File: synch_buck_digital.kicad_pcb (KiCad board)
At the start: 4 copper layers, 60 x 60 mm, 48 parts, among them U1 BSC066N06NSATMA1, U2 BSC066N06NSATMA1, U3 INA241A3IDDFR

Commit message: Updated pcb
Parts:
- moved TP4 16.0 mm to (235.1, 87.3)
- moved TP1 13.0 mm to (208.0, 89.3)
- moved C_OC_100P1 11.2 mm to (190.9, 87.1)
- moved C_OC_10N1 11.2 mm to (192.4, 87.9)
- moved C_OC_1U1 11.2 mm to (193.9, 87.1)
- moved R_HYS1 11.2 mm to (192.1, 90.7)
- moved U_OC1 11.2 mm to (188.0, 89.0)
- moved J_STM1 11.1 mm to (192.0, 99.6)
- moved TP3 8.14 mm to (203.9, 89.3)
- moved C_VFB_FILT1 5.82 mm to (233.5, 92.0)
- moved R1_VFB1 5.82 mm to (230.5, 92.0)
- moved R2_VFB1 5.82 mm to (230.5, 87.4)
- moved D1 5.82 mm to (237.0, 92.9)
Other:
- board size 60 x 60 mm -> 60 x 49.6 mm
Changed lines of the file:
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@@
 	(footprint "Capacitor_SMD:C_0603_1608Metric"
 		(layer "F.Cu")
-		(at 233.83 97.8525 90)
+		(at 233.47 92.04 90)
 		(descr "Capacitor SMD 0603 (1608 Metric), square (rectangular) end terminal, IPC-7351 nominal, (Body size source: IPC-SM-782 page 76, https://www.pcb-3d.com/wordpress/wp-content/uploads/ipc-sm-782a_amendment_1_and_2.pdf)")
 		(tags "capacitor")
@@
 	(footprint "Connector_PinHeader_2.54mm:PinHeader_1x13_P2.54mm_Vertical"
 		(layer "F.Cu")
-		(at 195.48 110.21 90)
+		(at 192.04 99.63 90)
 		(descr "Through hole straight pin header, 1x13, 2.54mm pitch, single row")
 		(tags "Through hole pin header THT 1x13 2.54mm single row")
@@
 	(footprint "TLV3603:SC70_DCK_TEX"
 		(layer "F.Cu")
-		(at 187.90755 100.159999)
+		(at 188.03755 88.999999)
 		(tags "TLV3603DCKR-ET ")
 		(property "Reference" "U_OC1"
@@
 	(footprint "Resistor_SMD:R_0603_1608Metric"
 		(layer "F.Cu")
-		(at 230.83 93.2325 -90)
+		(at 230.47 87.42 -90)
 		(descr "Resistor SMD 0603 (1608 Metric), square (rectangular) end terminal, IPC-7351 nominal, (Body size source: IPC-SM-782 page 72, https://www.pcb-3d.com/wordpress/wp-content/uploads/ipc-sm-782a_amendment_1_and_2.pdf)")
 		(tags "resistor")
@@
 	(footprint "Capacitor_SMD:C_0805_2012Metric"
 		(layer "F.Cu")
-		(at 193.78 98.28 90)
+		(at 193.91 87.12 90)
 		(descr "Capacitor SMD 0805 (2012 Metric), square (rectangular) end terminal, IPC-7351 nominal, (Body size source: IPC-SM-782 page 76, https://www.pcb-3d.com/wordpress/wp-content/uploads/ipc-sm-782a_amendment_1_and_2.pdf, https://docs.google.com/spreadsheets/d/1BsfQQcO9C6DZCsRaXUlFlo91Tg2WpOkGARC1WS5S8t0/edit?usp=sharing)")
 		(tags "capacitor")
@@
 	(footprint "Capacitor_SMD:C_0402_1005Metric"
 		(layer "F.Cu")
-		(at 192.3 99.02 90)
+		(at 192.43 87.86 90)
 		(descr "Capacitor SMD 0402 (1005 Metric), square (rectangular) end terminal, IPC-7351 nominal, (Body size source: IPC-SM-782 page 76, https://www.pcb-3d.com/wordpress/wp-content/uploads/ipc-sm-782a_amendment_1_and_2.pdf)")
 		(tags "capacitor")
@@
 	(footprint "Resistor_SMD:R_0603_1608Metric"
 		(layer "F.Cu")
-		(at 191.985 101.84 180)
+		(at 192.115 90.68 180)
 		(descr "Resistor SMD 0603 (1608 Metric), square (rectangular) end terminal, IPC-7351 nominal, (Body size source: IPC-SM-782 page 72, https://www.pcb-3d.com/wordpress/wp-content/uploads/ipc-sm-782a_amendment_1_and_2.pdf)")
 		(tags "resistor")
@@
 	(footprint "Diode_SMD:D_SOD-123"
 		(layer "F.Cu")
-		(at 237.32 98.7325 -90)
+		(at 236.96 92.92 -90)
 		(descr "SOD-123")
 		(tags "SOD-123")
@@
 	(footprint "Capacitor_SMD:C_0805_2012Metric"
 		(layer "F.Cu")
-		(at 190.8 98.25 90)
+		(at 190.93 87.09 90)
 		(descr "Capacitor SMD 0805 (2012 Metric), square (rectangular) end terminal, IPC-7351 nominal, (Body size source: IPC-SM-782 page 76, https://www.pcb-3d.com/wordpress/wp-content/uploads/ipc-sm-782a_amendment_1_and_2.pdf, https://docs.google.com/spreadsheets/d/1BsfQQcO9C6DZCsRaXUlFlo91Tg2WpOkGARC1WS5S8t0/edit?usp=sharing)")
 		(tags "capacitor")
@@
 	(footprint "TestPoint:TestPoint_Pad_2.0x2.0mm"
 		(layer "F.Cu")
-		(at 215.51 99.83)
+		(at 207.98 89.29)
 		(descr "SMD rectangular pad as test Point, square 2.0mm side length")
 		(tags "test point SMD pad rectangle square")
@@
 	(footprint "TestPoint:TestPoint_Pad_2.0x2.0mm"
 		(layer "F.Cu")
-		(at 224.07 98.88)
+		(at 235.05 87.29)
 		(descr "SMD rectangular pad as test Point, square 2.0mm side length")
 		(tags "test point SMD pad rectangle square")
@@
 	(footprint "Resistor_SMD:R_0603_1608Metric"
 		(layer "F.Cu")
-		(at 230.87 97.8625 90)
+		(at 230.51 92.05 90)
 		(descr "Resistor SMD 0603 (1608 Metric), square (rectangular) end terminal, IPC-7351 nominal, (Body size source: IPC-SM-782 page 72, https://www.pcb-3d.com/wordpress/wp-content/uploads/ipc-sm-782a_amendment_1_and_2.pdf)")
 		(tags "resistor")
@@
 	(footprint "TestPoint:TestPoint_Pad_2.0x2.0mm"
 		(layer "F.Cu")
-		(at 206.34 97.07)
+		(at 203.86 89.32)
 		(descr "SMD rectangular pad as test Point, square 2.0mm side length")
 		(tags "test point SMD pad rectangle square")
@@
 	(gr_rect
 		(start 180 54)
-		(end 240 114)
+		(end 240 103.59)
 		(stroke
 			(width 0.05)
@@
 		)
 		(min_thickness 0.25)
-		(fill yes
+		(fill
 			(thermal_gap 0.5)
 			(thermal_bridge_width 0.5)
@@
 		(polygon
 			(pts
-				(xy 180 83.75) (xy 180 114) (xy 240 114) (xy 240 84.07)
+				(xy 180 83.75) (xy 180 103.71) (xy 240 103.71) (xy 240 84.07)
 			)
 		)

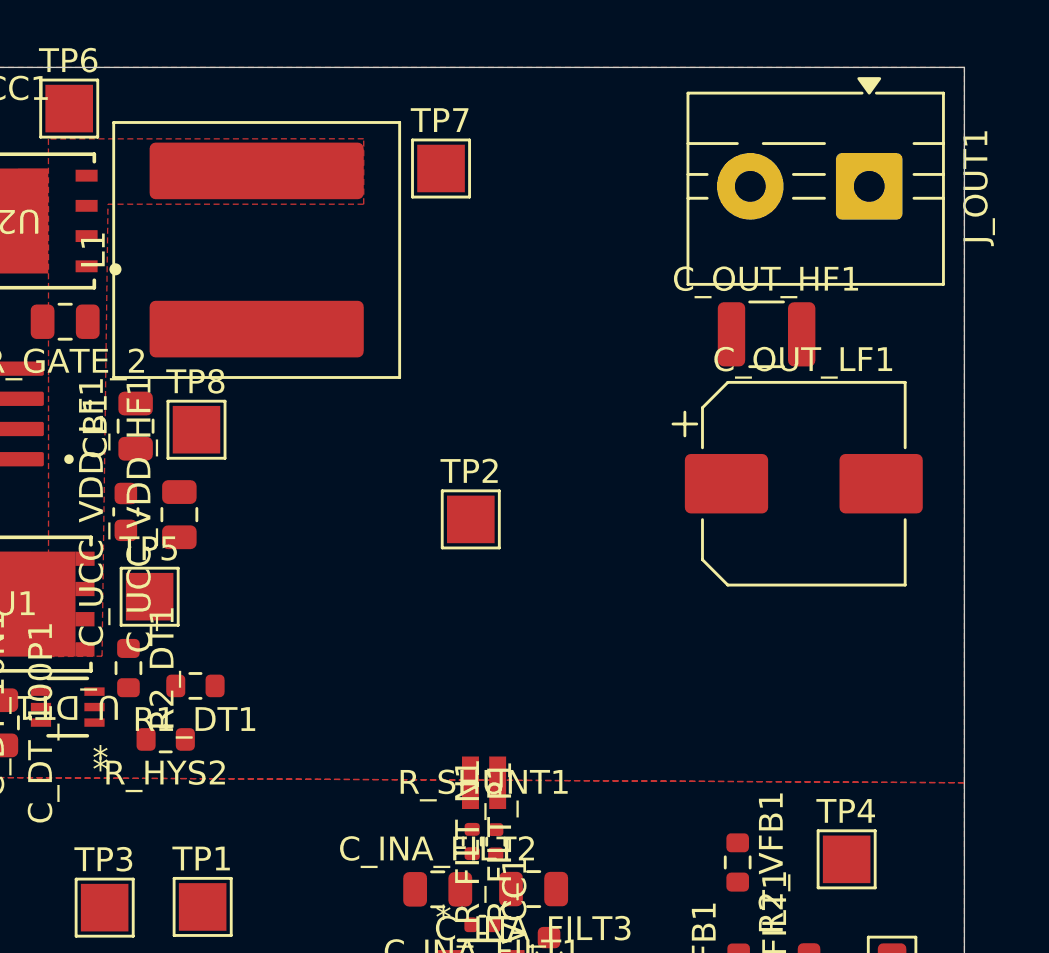
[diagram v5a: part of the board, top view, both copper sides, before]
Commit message: Updated pour topology
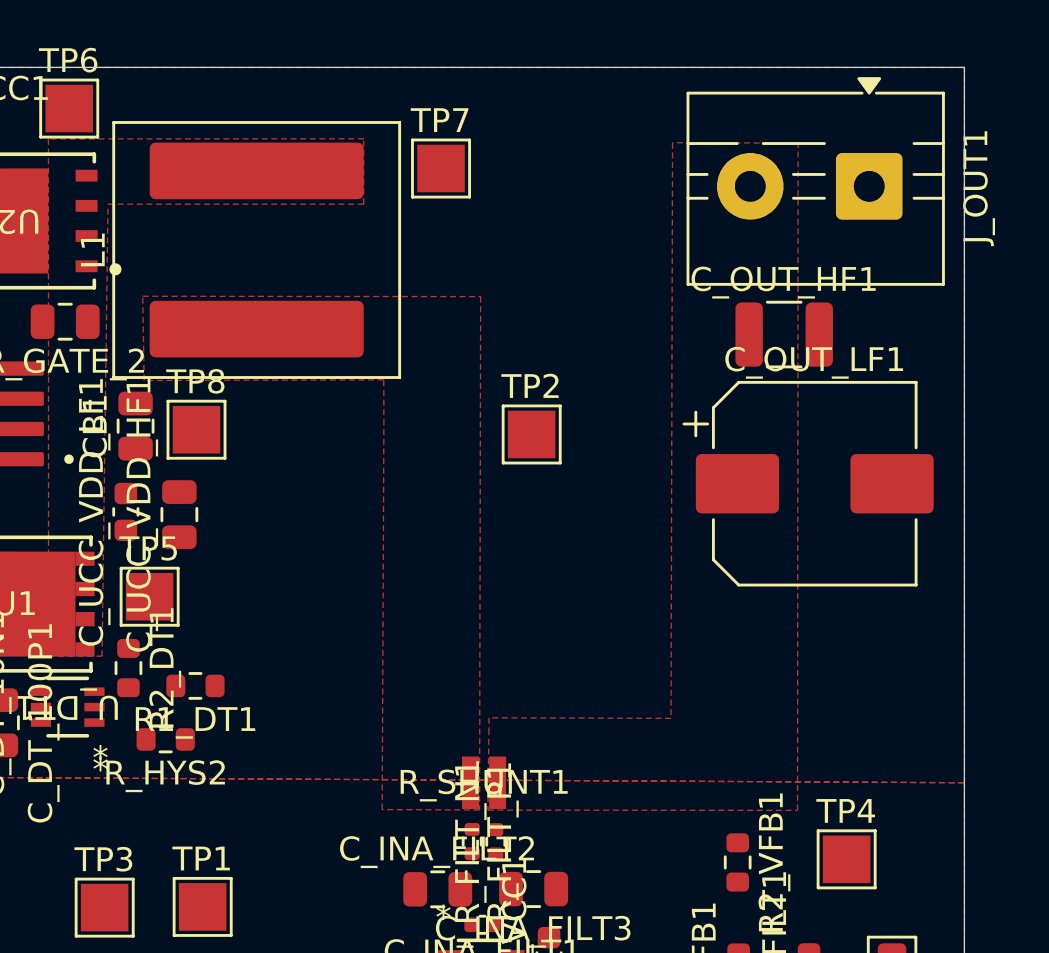
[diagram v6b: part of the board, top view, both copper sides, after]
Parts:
- moved TP2 4.39 mm to (221.8, 69.4)
- moved C_OUT_HF1 0.74 mm to (232.4, 65.2)
- moved C_OUT_LF1 0.46 mm to (233.7, 71.5)
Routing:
- added copper zone on F.Cu, net /SHUNT_N
- added copper zone on F.Cu, net /SHUNT_P
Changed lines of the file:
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@@
 		(capping no)
 		(filling no)
-		(zone_defaults)
 		(pcbplotparams
 			(layerselection 0x00000000_00000000_55555555_5755f5ff)
@@
 	(footprint "TestPoint:TestPoint_Pad_2.0x2.0mm"
 		(layer "F.Cu")
-		(at 219.25 73)
+		(at 221.81 69.43)
 		(descr "SMD rectangular pad as test Point, square 2.0mm side length")
 		(tags "test point SMD pad rectangle square")
@@
 	(footprint "Capacitor_SMD:C_1210_3225Metric"
 		(layer "F.Cu")
-		(at 231.685 65.22)
+		(at 232.425 65.23)
 		(descr "Capacitor SMD 1210 (3225 Metric), square (rectangular) end terminal, IPC-7351 nominal, (Body size source: IPC-SM-782 page 76, https://www.pcb-3d.com/wordpress/wp-content/uploads/ipc-sm-782a_amendment_1_and_2.pdf)")
 		(tags "capacitor")
@@
 	(footprint "Capacitor_SMD:CP_Elec_8x10"
 		(layer "F.Cu")
-		(at 233.25 71.5)
+		(at 233.71 71.5)
 		(descr "SMD capacitor, aluminum electrolytic, Nichicon, 8.0x10mm")
 		(tags "capacitor electrolytic")
@@
 			(thermal_gap 0.5)
 			(thermal_bridge_width 0.5)
+			(smoothing fillet)
+			(radius 1)
 			(island_removal_mode 0)
 		)
@@
 			)
 		)
+	)
+	(zone
+		(net "/SHUNT_P")
+		(layer "F.Cu")
+		(name "Shunt_P")
+		(hatch edge 0.5)
+		(priority 3)
+		(connect_pads yes
+			(clearance 0.5)
+		)
+		(min_thickness 0.25)
+		(fill
+			(thermal_gap 0.5)
+			(thermal_bridge_width 0.5)
+			(smoothing fillet)
+			(radius 3)
+			(island_removal_mode 0)
+		)
+		(polygon
+			(pts
+				(xy 205.52 67.16) (xy 205.46 63.62) (xy 219.665365 63.634449) (xy 219.618637 85.216566) (xy 215.525599 85.198429)
+				(xy 215.597263 69.025974) (xy 215.592363 67.133916)
+			)
+		)
+	)
+	(zone
+		(net "/SHUNT_N")
+		(layer "F.Cu")
+		(name "V_OUT")
+		(hatch edge 0.5)
+		(priority 4)
+		(connect_pads yes
+			(clearance 0.5)
+		)
+		(min_thickness 0.25)
+		(fill
+			(thermal_gap 0.5)
+			(thermal_bridge_width 0.5)
+			(smoothing fillet)
+			(radius 3)
+			(island_removal_mode 0)
+		)
+		(polygon
+			(pts
+				(xy 219.97 85.22) (xy 232.986244 85.231023) (xy 233.01 57.18) (xy 227.731625 57.166182) (xy 227.668281 81.363943)
+				(xy 220.02 81.34) (xy 220.013417 81.820561)
+			)
+		)

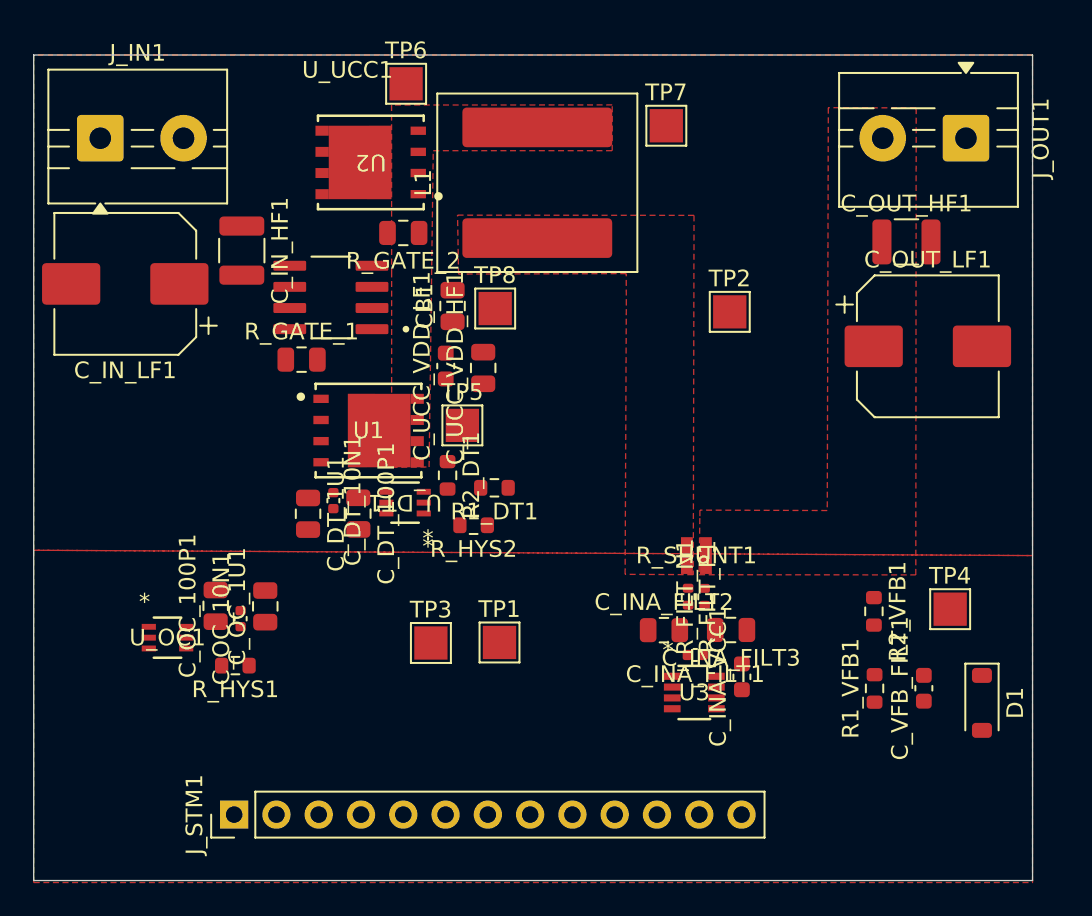
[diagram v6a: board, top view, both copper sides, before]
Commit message: Signal Traces Added
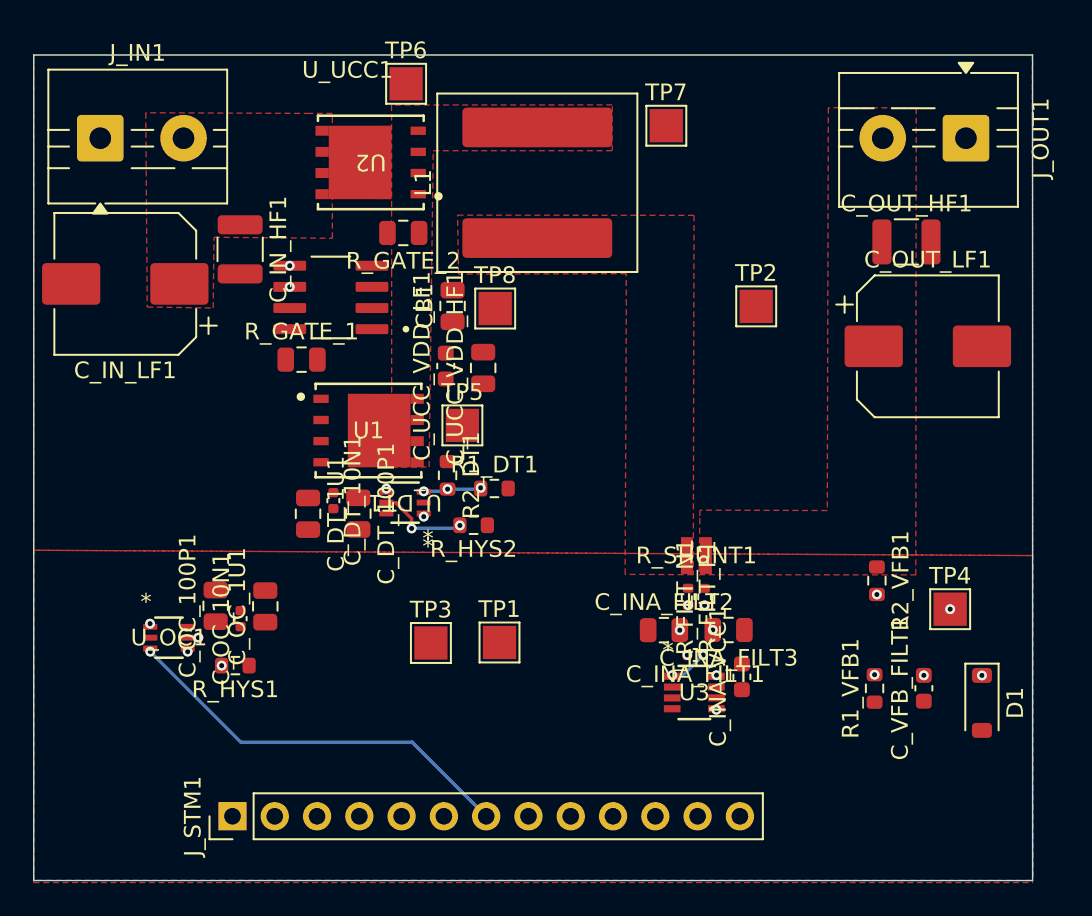
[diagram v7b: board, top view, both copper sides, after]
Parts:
- moved R2_VFB1 1.85 mm to (230.7, 85.6)
- moved TP2 1.62 mm to (223.4, 69.1)
- moved C_INA_FILT3 0.15 mm to (221.7, 88.5)
- moved J_STM1 0.14 mm to (191.9, 99.7)
- moved C_IN_HF1 0.12 mm to (192.4, 65.7)
- moved U_OC1 0.09 mm to (188.1, 89.0)
- turned R1_DT1 to 0 degrees
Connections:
- J_STM1 pad 1: /DT_REF -> /PROT_OUT
- J_STM1 pad 2: /COMP_OUT -> /PROT_REF
- J_STM1 pad 3: /PROT_OUT -> /PWM_LS
- J_STM1 pad 4: /PROT_REF -> /PWM_HS
- J_STM1 pad 5: /PWM_LS -> /DT_REF
- J_STM1 pad 6: /PWM_HS -> /COMP_OUT
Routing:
- net /SENSE_OUT: track 0.00 -> 40.9 mm, vias 0 -> 2
- net /V_FB: track 0.00 -> 39.9 mm, vias 0 -> 5
- net /PWM_HS: track 0.00 -> 35.0 mm, vias 0 -> 1
- net /PWM_LS: track 0.00 -> 33.9 mm, vias 0 -> 1
- net /DT_REF: track 0.00 -> 20.1 mm, vias 0 -> 1
- net /COMP_OUT: track 0.00 -> 18.5 mm, vias 0 -> 1
- net /PROT_OUT: track 0.00 -> 15.7 mm, vias 0 -> 1
- net /PROT_REF: track 0.00 -> 12.1 mm, vias 0 -> 1
- net Net-(U3-IN-): track 0.00 -> 5.94 mm, vias 0 -> 4
- net Net-(U3-IN+): track 0.00 -> 5.64 mm, vias 0 -> 4
- net Net-(U_DT1-*LE/HYS): track 0.00 -> 5.49 mm, vias 0 -> 2
- net Net-(U_DT1-IN+): track 0.00 -> 3.54 mm, vias 0 -> 3
- net Net-(U_OC1-*LE/HYS): track 0.00 -> 2.90 mm, vias 0 -> 2
- added copper zone on F.Cu, net +12V
- added copper zone on B.Cu, net PGND
- added copper zone on In1.Cu, net PGND

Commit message: More Traces
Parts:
- moved TP7 2.42 mm to (220.4, 58.4)
- moved C_OC_10N1 0.23 mm to (192.4, 87.6)
- moved C_OC_100P1 0.14 mm to (190.9, 87.2)
- moved C_OC_1U1 0.12 mm to (193.9, 87.2)
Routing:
- net +5V: track 0.00 -> 58.6 mm
- net /SW: track 0.00 -> 10.2 mm
- net /SHUNT_N: track 0.00 -> 2.00 mm
- net /SHUNT_P: track 0.00 -> 1.99 mm
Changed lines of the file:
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@@
 	(footprint "Capacitor_SMD:C_0805_2012Metric"
 		(layer "F.Cu")
-		(at 193.91 87.12 90)
+		(at 193.9 87.24 90)
 		(descr "Capacitor SMD 0805 (2012 Metric), square (rectangular) end terminal, IPC-7351 nominal, (Body size source: IPC-SM-782 page 76, https://www.pcb-3d.com/wordpress/wp-content/uploads/ipc-sm-782a_amendment_1_and_2.pdf, https://docs.google.com/spreadsheets/d/1BsfQQcO9C6DZCsRaXUlFlo91Tg2WpOkGARC1WS5S8t0/edit?usp=sharing)")
 		(tags "capacitor")
@@
 	(footprint "TestPoint:TestPoint_Pad_2.0x2.0mm"
 		(layer "F.Cu")
-		(at 218 58.25)
+		(at 220.42 58.35)
 		(descr "SMD rectangular pad as test Point, square 2.0mm side length")
 		(tags "test point SMD pad rectangle square")
@@
 	(footprint "Capacitor_SMD:C_0402_1005Metric"
 		(layer "F.Cu")
-		(at 192.43 87.86 90)
+		(at 192.44 87.63 90)
 		(descr "Capacitor SMD 0402 (1005 Metric), square (rectangular) end terminal, IPC-7351 nominal, (Body size source: IPC-SM-782 page 76, https://www.pcb-3d.com/wordpress/wp-content/uploads/ipc-sm-782a_amendment_1_and_2.pdf)")
 		(tags "capacitor")
@@
 	(footprint "Capacitor_SMD:C_0805_2012Metric"
 		(layer "F.Cu")
-		(at 190.93 87.09 90)
+		(at 190.94 87.23 90)
 		(descr "Capacitor SMD 0805 (2012 Metric), square (rectangular) end terminal, IPC-7351 nominal, (Body size source: IPC-SM-782 page 76, https://www.pcb-3d.com/wordpress/wp-content/uploads/ipc-sm-782a_amendment_1_and_2.pdf, https://docs.google.com/spreadsheets/d/1BsfQQcO9C6DZCsRaXUlFlo91Tg2WpOkGARC1WS5S8t0/edit?usp=sharing)")
 		(tags "capacitor")
@@
 	)
 	(segment
+		(start 196.48 80.61)
+		(end 197.68 80.61)
+		(width 0.2)
+		(layer "F.Cu")
+		(net "+5V")
+	)
+	(segment
+		(start 196.48 80.61)
+		(end 196.48 81.000256)
+		(width 0.2)
+		(layer "F.Cu")
+		(net "+5V")
+	)
+	(segment
+		(start 199.85 84.370256)
+		(end 199.85 88.19)
+		(width 0.2)
+		(layer "F.Cu")
+		(net "+5V")
+	)
+	(segment
+		(start 190.94 88.18)
+		(end 191.01 88.11)
+		(width 0.2)
+		(layer "F.Cu")
+		(net "+5V")
+	)
+	(segment
+		(start 201.85 90.21)
+		(end 211.37 99.73)
+		(width 0.2)
+		(layer "F.Cu")
+		(net "+5V")
+	)
+	(segment
+		(start 198.31 80.6)
+		(end 198 80.29)
+		(width 0.2)
+		(layer "F.Cu")
+		(net "+5V")
+	)
+	(segment
+		(start 190.77 88.35)
+		(end 190.94 88.18)
+		(width 0.2)
+		(layer "F.Cu")
+		(net "+5V")
+	)
+	(segment
+		(start 192.44 88.11)
+		(end 193.82 88.11)
+		(width 0.2)
+		(layer "F.Cu")
+		(net "+5V")
+	)
+	(segment
+		(start 199.85 88.19)
+		(end 201.85 90.19)
+		(width 0.2)
+		(layer "F.Cu")
+		(net "+5V")
+	)
+	(segment
+		(start 203.86 89.32)
+		(end 200.98 89.32)
+		(width 0.2)
+		(layer "F.Cu")
+		(net "+5V")
+	)
+	(segment
+		(start 214.39 98.58)
+		(end 213.41 98.58)
+		(width 0.2)
+		(layer "F.Cu")
+		(net "+5V")
+	)
+	(segment
+		(start 191.01 88.11)
+		(end 192.44 88.11)
+		(width 0.2)
+		(layer "F.Cu")
+		(net "+5V")
+	)
+	(segment
+		(start 189.2479 88.35)
+		(end 190.77 88.35)
+		(width 0.2)
+		(layer "F.Cu")
+		(net "+5V")
+	)
+	(segment
+		(start 221.01 92.62)
+		(end 222.05 92.62)
+		(width 0.2)
+		(layer "F.Cu")
+		(net "+5V")
+	)
+	(segment
+		(start 193.87 88.11)
+		(end 193.91 88.07)
+		(width 0.2)
+		(layer "F.Cu")
+		(net "+5V")
+	)
+	(segment
+		(start 196.48 81.000256)
+		(end 199.85 84.370256)
+		(width 0.2)
+		(layer "F.Cu")
+		(net "+5V")
+	)
+	(segment
+		(start 201.85 90.19)
+		(end 201.85 90.21)
+		(width 0.2)
+		(layer "F.Cu")
+		(net "+5V")
+	)
+	(segment
+		(start 199.5 80.6)
+		(end 198.31 80.6)
+		(width 0.2)
+		(layer "F.Cu")
+		(net "+5V")
+	)
+	(segment
+		(start 221.01 92.62)
+		(end 220.35 92.62)
+		(width 0.2)
+		(layer "F.Cu")
+		(net "+5V")
+	)
+	(segment
+		(start 193.9 88.19)
+		(end 199.85 88.19)
+		(width 0.2)
+		(layer "F.Cu")
+		(net "+5V")
+	)
+	(segment
+		(start 199.5 80.6)
+		(end 200.439998 81.539998)
+		(width 0.2)
+		(layer "F.Cu")
+		(net "+5V")
+	)
+	(segment
+		(start 220.35 92.62)
+		(end 214.39 98.58)
+		(width 0.2)
+		(layer "F.Cu")
+		(net "+5V")
+	)
+	(segment
+		(start 213.41 98.58)
+		(end 212.26 99.73)
+		(width 0.2)
+		(layer "F.Cu")
+		(net "+5V")
+	)
+	(segment
+		(start 197.68 80.61)
+		(end 198 80.29)
+		(width 0.2)
+		(layer "F.Cu")
+		(net "+5V")
+	)
+	(segment
+		(start 193.82 88.11)
+		(end 193.9 88.19)
+		(width 0.2)
+		(layer "F.Cu")
+		(net "+5V")
+	)
+	(segment
+		(start 222.05 92.62)
+		(end 222.54 92.13)
+		(width 0.2)
+		(layer "F.Cu")
+		(net "+5V")
+	)
+	(segment
+		(start 200.439998 81.539998)
+		(end 201.1821 81.539998)
+		(width 0.2)
+		(layer "F.Cu")
+		(net "+5V")
+	)
+	(segment
+		(start 211.37 99.73)
+		(end 212.26 99.73)
+		(width 0.2)
+		(layer "F.Cu")
+		(net "+5V")
+	)
+	(segment
 		(start 230.47 86.595)
 		(end 230.47 86.6)
@@
 	)
 	(segment
+		(start 220.38 85.96)
+		(end 220.3 86.04)
+		(width 0.2)
+		(layer "F.Cu")
+		(net "/SHUNT_N")
+	)
+	(segment
+		(start 220.38 84.07)
+		(end 220.38 85.96)
+		(width 0.2)
+		(layer "F.Cu")
+		(net "/SHUNT_N")
+	)
+	(segment
+		(start 219.237 85.957)
+		(end 219.31 86.03)
+		(width 0.2)
+		(layer "F.Cu")
+		(net "/SHUNT_P")
+	)
+	(segment
+		(start 219.237 84.07)
+		(end 219.237 85.957)
+		(width 0.2)
+		(layer "F.Cu")
+		(net "/SHUNT_P")
+	)
+	(segment
+		(start 220.42 58.35)
+		(end 210.25 58.35)
+		(width 0.2)
+		(layer "F.Cu")
+		(net "/SW")
+	)
+	(segment
